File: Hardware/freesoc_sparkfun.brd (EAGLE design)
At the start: 116.8 x 53.3 mm, 94 parts, among them J1 POWER_JACKPTH, U1 CY8C5868AXI-LP035, U2 MIC5219 5V, U3 MIC5219 3.3V, U7 CY8C5868LTI-LP039, Y1 32.768kHz

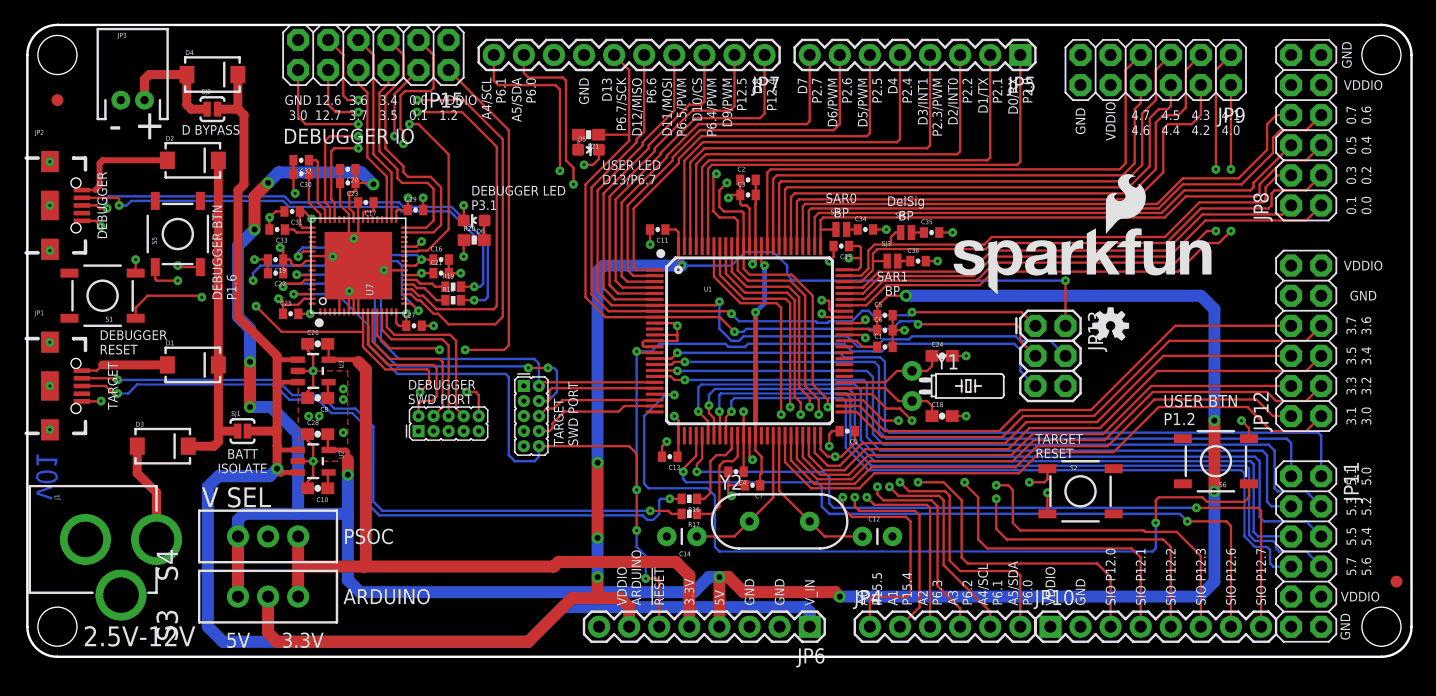
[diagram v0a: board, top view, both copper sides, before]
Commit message: Files changed after v01 feedback, to add kitprog ID pins
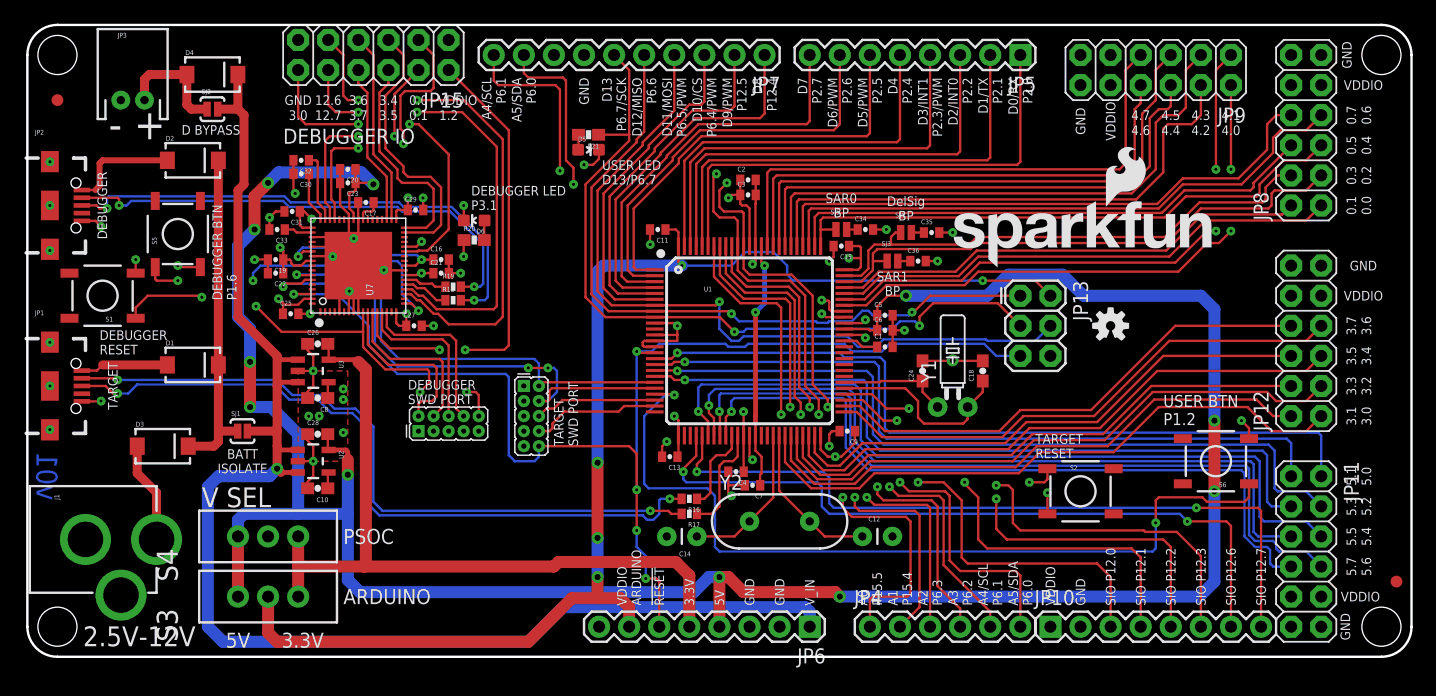
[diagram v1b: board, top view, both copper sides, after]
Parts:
- moved C18 5.13 mm to (80.6, 24.1), turned to 90 degrees
- moved Y1 3.86 mm to (78.1, 21.1), turned to 0 degrees
- moved JP13 2.84 mm to (83.8, 30.5)
- moved LOGO1 2.29 mm to (77.5, 32.8)
- moved C24 2.08 mm to (75.6, 24.1), turned to 90 degrees
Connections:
- net GND: now also U7.54, U7.56
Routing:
- net GND: track 121.9 -> 133.8 mm, vias 48 -> 47
- net P15.2: track 8.88 -> 16.4 mm
- net VDDIO_ARDUINO: track 114.5 -> 109.9 mm
- net D11: track 67.0 -> 65.5 mm
- net 5V: track 214.6 -> 216.1 mm
- net D12: track 61.7 -> 60.5 mm
- net D13: track 66.4 -> 65.5 mm
- net !RESET: track 119.7 -> 119.0 mm
- net P15.3: track 8.83 -> 9.37 mm

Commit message: Changes for v02 in, review
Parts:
- moved C30 2.17 mm to (22.4, 38.7)
- moved C32 2.17 mm to (22.4, 39.9)
- moved C18 1.42 mm to (81.3, 22.9), turned to 180 degrees
- moved C17 1.02 mm to (29.5, 38.9), turned to 0 degrees
- moved C24 0.63 mm to (74.9, 24.1), turned to 0 degrees
- moved C20 0.52 mm to (27.6, 41.3), turned to 0 degrees
- moved C23 0.52 mm to (27.6, 40.1), turned to 0 degrees
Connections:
- net !RESET: now also U7.3; no longer U7.66
- net P1.0: now also U7.46; no longer U7.62
- net P1.1: now also U7.47; no longer U7.63
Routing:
- net P1.0: track 39.7 -> 47.4 mm
- net !RESET: track 119.0 -> 114.4 mm
- net P1.1: track 46.7 -> 50.4 mm
- net GND: track 133.8 -> 136.2 mm, vias 47 -> 46
- net 5V: track 216.1 -> 213.7 mm
- net DEBUG_D-_BUS: track 41.4 -> 43.7 mm
- net DEBUG_D+_BUS: track 44.1 -> 46.5 mm
- net P15.3: track 9.37 -> 11.0 mm
- net DEBUG_SAR1_BP: track 5.92 -> 4.29 mm
- net P15.2: track 16.4 -> 17.9 mm
- net DEBUG_P0.0: track 24.0 -> 25.6 mm
- net DEBUG_DS_BP: track 4.25 -> 2.90 mm
- net DEBUG_P0.1: track 19.2 -> 19.9 mm
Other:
- board text added: "PSoC5LP Development Board"

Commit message: ready for protos v02
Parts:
- moved FID2 8.13 mm to (8.89, 52.1)
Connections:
- removed net P1.5: U1.25
- removed net P1.6: U1.27
- removed net P1.7: U1.28
- net GND: now also JP10.1; no longer JP10.2
- net VDDIO: now also JP10.2; no longer JP10.1
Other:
- board text added: "1"
- board text added: "2"
- board text added: "3"
- board text added: "4"
- board text added: "LAYER NUMBERS"
- board text added: "Measurement units given in inches"
- board text added: "NC"
- board text removed: "PSOC"
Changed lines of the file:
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@@
 <layers>
 <layer number="1" name="Top" color="4" fill="1" visible="yes" active="yes"/>
-<layer number="2" name="Route2" color="1" fill="3" visible="no" active="yes"/>
-<layer number="15" name="Route15" color="4" fill="6" visible="no" active="yes"/>
+<layer number="2" name="Route2" color="1" fill="3" visible="yes" active="yes"/>
+<layer number="15" name="Route15" color="4" fill="6" visible="yes" active="yes"/>
 <layer number="16" name="Bottom" color="1" fill="1" visible="yes" active="yes"/>
 <layer number="17" name="Pads" color="2" fill="1" visible="yes" active="yes"/>
@@
 <layer number="28" name="bValues" color="7" fill="1" visible="no" active="yes"/>
 <layer number="29" name="tStop" color="7" fill="3" visible="no" active="yes"/>
-<layer number="30" name="bStop" color="7" fill="6" visible="yes" active="yes"/>
+<layer number="30" name="bStop" color="7" fill="6" visible="no" active="yes"/>
 <layer number="31" name="tCream" color="7" fill="4" visible="no" active="yes"/>
 <layer number="32" name="bCream" color="7" fill="5" visible="no" active="yes"/>
@@
 <layer number="45" name="Holes" color="7" fill="1" visible="yes" active="yes"/>
 <layer number="46" name="Milling" color="3" fill="1" visible="no" active="yes"/>
-<layer number="47" name="Measures" color="7" fill="1" visible="no" active="yes"/>
+<layer number="47" name="Measures" color="7" fill="1" visible="yes" active="yes"/>
 <layer number="51" name="tDocu" color="6" fill="1" visible="yes" active="yes"/>
 <layer number="52" name="bDocu" color="7" fill="1" visible="no" active="no"/>
@@
 <text x="6.858" y="43.688" size="2.54" layer="21" font="vector" ratio="15">-</text>
 <text x="4.699" y="0.889" size="1.6764" layer="21" font="vector" ratio="15">2.5V-12V</text>
-<text x="26.67" y="10.16" size="1.27" layer="21" font="vector" ratio="15" align="center-left">PSOC</text>
+<text x="26.67" y="10.16" size="1.27" layer="21" font="vector" ratio="15" align="center-left">VDDIO</text>
 <text x="26.67" y="5.08" size="1.27" layer="21" font="vector" ratio="15" align="center-left">ARDUINO</text>
 <text x="14.732" y="13.462" size="1.6764" layer="21" font="vector" ratio="15" align="center-left">V SEL</text>
@@
 <text x="113.03" y="10.16" size="0.8128" layer="21" font="vector" ratio="15" rot="R90" align="center">5.4</text>
 <text x="111.379" y="50.8" size="0.8128" layer="21" font="vector" ratio="15" rot="R90" align="center">GND</text>
-<text x="86.36" y="4.318" size="0.8128" layer="21" font="vector" ratio="15" rot="R90" align="center-left">VDDIO</text>
-<text x="88.9" y="4.318" size="0.8128" layer="21" font="vector" ratio="15" rot="R90" align="center-left">GND</text>
+<text x="88.9" y="4.318" size="0.8128" layer="21" font="vector" ratio="15" rot="R90" align="center-left">VDDIO</text>
+<text x="86.36" y="4.318" size="0.8128" layer="21" font="vector" ratio="15" rot="R90" align="center-left">GND</text>
 <text x="91.44" y="4.318" size="0.8128" layer="21" font="vector" ratio="15" rot="R90" align="center-left">SIO P12.0</text>
 <text x="93.98" y="4.318" size="0.8128" layer="21" font="vector" ratio="15" rot="R90" align="center-left">SIO P12.1</text>
@@
 ISOLATE</text>
 <text x="2.54" y="15.24" size="1.778" layer="16" font="vector" ratio="15" rot="MR270" align="bottom-center">v01</text>
-<dimension x1="0" y1="50.8" x2="116.84" y2="48.26" x3="58.42" y3="58.42" textsize="1.778" textratio="15" layer="51" dtype="horizontal" unit="inch"/>
-<dimension x1="114.3" y1="0" x2="114.3" y2="53.34" x3="129.54" y3="26.67" textsize="1.778" textratio="15" layer="51" dtype="horizontal" unit="inch"/>
-<dimension x1="0" y1="2.54" x2="2.54" y2="2.54" x3="1.27" y3="-3.81" textsize="1.778" textratio="15" layer="51" dtype="horizontal" unit="inch"/>
-<dimension x1="0" y1="2.54" x2="114.3" y2="2.54" x3="57.15" y3="-8.89" textsize="1.778" textratio="15" layer="51" dtype="horizontal" unit="inch"/>
-<dimension x1="2.54" y1="0" x2="2.54" y2="2.54" x3="-7.62" y3="1.27" textsize="1.778" textratio="15" layer="51" dtype="horizontal" unit="inch"/>
-<dimension x1="2.54" y1="0" x2="2.54" y2="50.8" x3="-12.7" y3="25.4" textsize="1.778" textratio="15" layer="51" dtype="horizontal" unit="inch"/>
+<dimension x1="0" y1="50.8" x2="116.84" y2="48.26" x3="58.42" y3="58.42" textsize="1.778" textratio="15" layer="47" dtype="horizontal" unit="inch"/>
+<dimension x1="114.3" y1="0" x2="114.3" y2="53.34" x3="129.54" y3="26.67" textsize="1.778" textratio="15" layer="47" dtype="horizontal" unit="inch"/>
+<dimension x1="0" y1="2.54" x2="2.54" y2="2.54" x3="1.27" y3="-3.81" textsize="1.778" textratio="15" layer="47" dtype="horizontal" unit="inch"/>
+<dimension x1="0" y1="2.54" x2="114.3" y2="2.54" x3="57.15" y3="-8.89" textsize="1.778" textratio="15" layer="47" dtype="horizontal" unit="inch"/>
+<dimension x1="2.54" y1="0" x2="2.54" y2="2.54" x3="-7.62" y3="1.27" textsize="1.778" textratio="15" layer="47" dtype="horizontal" unit="inch"/>
+<dimension x1="2.54" y1="0" x2="2.54" y2="50.8" x3="-12.7" y3="25.4" textsize="1.778" textratio="15" layer="47" dtype="horizontal" unit="inch"/>
 <text x="52.07" y="-27.94" size="1.778" layer="51" font="vector" ratio="15" align="bottom-center">M. Hord</text>
 <text x="73.025" y="30.48" size="0.8128" layer="21" font="vector" ratio="15" align="bottom-center">SAR1
@@
 <circle x="95.25" y="11.303" radius="0.40160625" width="0" layer="30"/>
 <circle x="12.7" y="31.75" radius="0.40160625" width="0" layer="30"/>
+<text x="0" y="-13.97" size="1.778" layer="47" font="vector" ratio="15">Measurement units given in inches</text>
+<text x="1.27" y="46.99" size="1.778" layer="1" font="vector" ratio="15">1</text>
+<text x="3.81" y="46.99" size="1.778" layer="2" font="vector" ratio="15">2</text>
+<text x="1.27" y="44.45" size="1.778" layer="15" font="vector" ratio="15">3</text>
+<text x="3.81" y="44.45" size="1.778" layer="16" font="vector" ratio="15">4</text>
+<text x="-11.43" y="44.45" size="1.778" layer="51" font="vector" ratio="15">LAYER
+NUMBERS</text>
+<wire x1="-2.921" y1="47.879" x2="-0.381" y2="47.879" width="0.254" layer="51"/>
+<wire x1="-1.016" y1="47.625" x2="-0.381" y2="47.879" width="0.254" layer="51"/>
+<wire x1="-0.381" y1="47.879" x2="-1.016" y2="48.133" width="0.254" layer="51"/>
+<text x="44.45" y="48.895" size="0.8128" layer="21" font="vector" ratio="15" rot="R90" align="center-right">NC</text>
+<text x="48.26" y="4.318" size="0.8128" layer="21" font="vector" ratio="15" rot="R90" align="center-left">NC</text>
 </plain>
 <attributes>
@@
 <element name="U$1" library="SparkFun-Aesthetics" package="FOUR_LAYER_WARNING" value="FOUR_LAYER_WARNING" x="15.24" y="-2.159"/>
 <element name="FID1" library="SparkFun-Aesthetics" package="FIDUCIAL-1X2" value="FIDUCIAL1X2" x="115.57" y="6.35"/>
-<element name="FID2" library="SparkFun-Aesthetics" package="FIDUCIAL-1X2" value="FIDUCIAL1X2" x="2.54" y="46.99"/>
+<element name="FID2" library="SparkFun-Aesthetics" package="FIDUCIAL-1X2" value="FIDUCIAL1X2" x="8.89" y="52.07"/>
 <element name="LOGO1" library="SparkFun-Aesthetics" package="SFE_LOGO_NAME_FLAME_.2" value="SFE_LOGO_NAME_FLAME.2_INCH" x="77.47" y="32.766"/>
 <element name="LOGO2" library="SparkFun-Aesthetics" package="OSHW-LOGO-S" value="OSHW-LOGOS" x="91.44" y="27.94"/>
@@
 <via x="21.209" y="30.226" extent="1-16" drill="0.254"/>
 <wire x1="22.86" y1="29.718" x2="21.59" y2="29.718" width="0.2032" layer="1"/>
-<contactref element="JP10" pad="1"/>
 <wire x1="60.46" y1="18.67" x2="60.46" y2="15.628" width="0.2032" layer="1"/>
 <wire x1="60.46" y1="15.628" x2="60.467" y2="15.621" width="0.2032" layer="1"/>
+<contactref element="JP10" pad="2"/>
 </signal>
 <signal name="GND">
@@
 <wire x1="76.977" y1="35.814" x2="78.105" y2="35.814" width="0.2032" layer="1"/>
 <via x="78.105" y="35.814" extent="1-16" drill="0.254"/>
-<contactref element="JP10" pad="2"/>
 <wire x1="59.167" y1="15.621" x2="59.167" y2="14.478" width="0.2032" layer="1"/>
 <wire x1="59.167" y1="14.478" x2="59.167" y2="13.858" width="0.2032" layer="1"/>
-<wire x1="59.167" y1="13.858" x2="59.436" y2="13.589" width="0.2032" layer="1"/>
-<via x="59.436" y="13.589" extent="1-16" drill="0.254"/>
+<wire x1="59.167" y1="13.858" x2="59.182" y2="13.843" width="0.2032" layer="1"/>
+<via x="59.182" y="13.843" extent="1-16" drill="0.254"/>
 <wire x1="60.564" y1="14.478" x2="59.167" y2="14.478" width="0.2032" layer="1"/>
 <wire x1="48.248" y1="42.799" x2="48.248" y2="42.025" width="0.2032" layer="1"/>
@@
 <wire x1="30.114" y1="39.609" x2="29.591" y2="40.132" width="0.2032" layer="1"/>
 <wire x1="29.591" y1="40.132" x2="28.209" y2="40.132" width="0.2032" layer="1"/>
+<contactref element="JP10" pad="1"/>
 </signal>
 <signal name="N$13">
@@
 <wire x1="44.069" y1="19.05" x2="43.18" y2="19.05" width="0.2032" layer="1"/>
 </signal>
-<signal name="P1.5">
-<contactref element="U1" pad="25"/>
-</signal>
-<signal name="P1.6">
-<contactref element="U1" pad="27"/>
-</signal>
-<signal name="P1.7">
-<contactref element="U1" pad="28"/>
-</signal>
 <signal name="P5.0">

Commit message: Up to V02, checklist and peer review completed
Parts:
- removed J1: POWER_JACKPTH, SparkFun-Connectors:POWER_JACK_PTH
- added JP18: POWER_JACKPTH_LOCK, SparkFun-Connectors:POWER_JACK_PTH_LOCK
- FRAME1, FRAME2, FRAME3: value FRAME-LETTER -> (none)
- JP11, JP12, JP15, JP8, JP9: value 2X6 FEMALE PTH -> 2X6 FEMALE
- S3, S4: device SparkFun-Electromechanical:SWITCH-SPDT -> SparkFun-Electromechanical:SWITCH-SPDT_LOCK.007S
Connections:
- net GND: now also JP18.GND, JP18.GNDBREAK; no longer J1.GND, J1.GNDBREAK
- net N$13: now also JP18.PWR; no longer J1.PWR
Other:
- board text removed: "M. Hord"
- board text removed: "v01"

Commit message: v10 almost ready
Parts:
- added C37, C38: 0.1uF, SparkFun-Capacitors:0402-CAP
- added R1, R2: 4.7K, SparkFun-Resistors:0603-RES
- added R3, R4: 10K, SparkFun-Resistors:0603-RES
- added R5, R6: 20k, SparkFun-Resistors:0603-RES
- U1: value CY8C5868AXI-LP035 -> CY8C5888AXI-LP035
- moved C13 1.66 mm to (53.3, 18.3), turned to 270 degrees
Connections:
- removed net DEBUG_USER_BTN: S5.1, U7.18
- removed net N$15: D1.A, JP1.VBUS1
- new net DEBUG_BTN: S5.1, U7.64
- new net V_BUS_DEBUG: R4.2, R5.2, U7.18
- new net V_BUS_HOST: R3.2, R6.2, U1.27
- new net V_HOST: D1.A, JP1.VBUS1, R3.1
- net !DEBUG_RESET: now also C38.1, R2.1
- net !RESET: now also C37.1, R1.1
- net 3.3V: now also C19.1, C2.1, C21.1, C22.1, C3.1, C4.1, R1.2, R2.2, U1.37, U1.88, U7.24, U7.59
- net GND: now also C37.2, C38.2, R5.1, R6.1
- net VDDIO: no longer C19.1, C2.1, C21.1, C22.1, C3.1, C4.1, U1.37, U1.88, U7.24, U7.59
- net V_DEBUG: now also R4.1
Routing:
- net 3.3V: track 64.4 -> 164.7 mm, vias 0 -> 7
- net V_BUS_HOST: track 0.00 -> 63.2 mm, vias 0 -> 2
- net V_BUS_DEBUG: track 0.00 -> 34.6 mm, vias 0 -> 2
- net DEBUG_USER_BTN: track 28.9 -> 0.00 mm, vias 3 -> 0
- net DEBUG_BTN: track 0.00 -> 28.5 mm, vias 0 -> 2
- net !RESET: track 114.4 -> 135.8 mm
- net VDDIO: track 47.9 -> 30.5 mm, vias 11 -> 7
- net V_HOST: track 0.00 -> 11.0 mm
- net N$15: track 7.41 -> 0.00 mm
- net GND: track 135.9 -> 142.6 mm, vias 46 -> 49
- net !DEBUG_RESET: track 40.1 -> 45.0 mm
- net V_DEBUG: track 9.37 -> 11.1 mm
- net 5V: track 213.8 -> 214.4 mm
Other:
- board text added: "ARDUINO VDDIO2"
- board text added: "DEBUGGER BTN P2.2"
- board text added: "VDDIO 0 1 3"
- board text removed: "ARDUINO"
- board text removed: "DEBUGGER BTN P1.6"
